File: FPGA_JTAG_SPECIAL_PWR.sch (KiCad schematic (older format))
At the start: 36 parts, among them J2 Reset_Switch, U900 GW1N-9LQ100

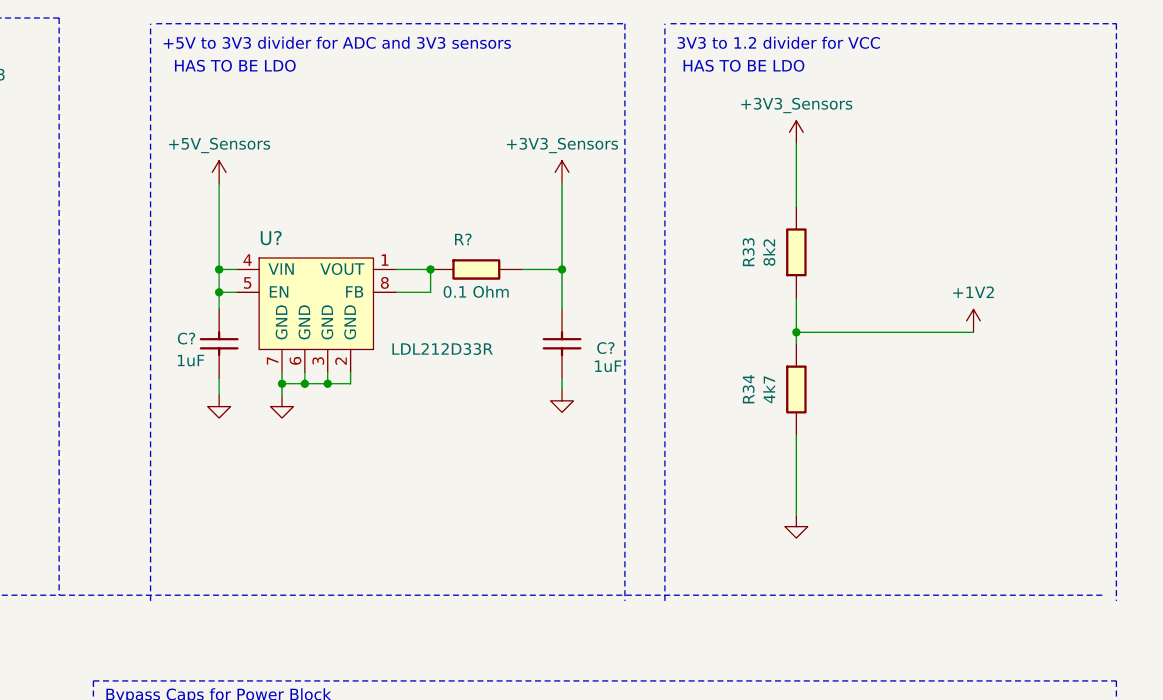
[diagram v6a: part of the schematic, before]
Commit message: TLV75512 ON fpga jtag special PWR sheet 7 Changed Q2 on Buzzer LEDs sheet 8 from N type to P type
TLV75512 ON fpga jtag special PWR sheet 7
Changed Q2 on Buzzer LEDs sheet 8 from N type to P type
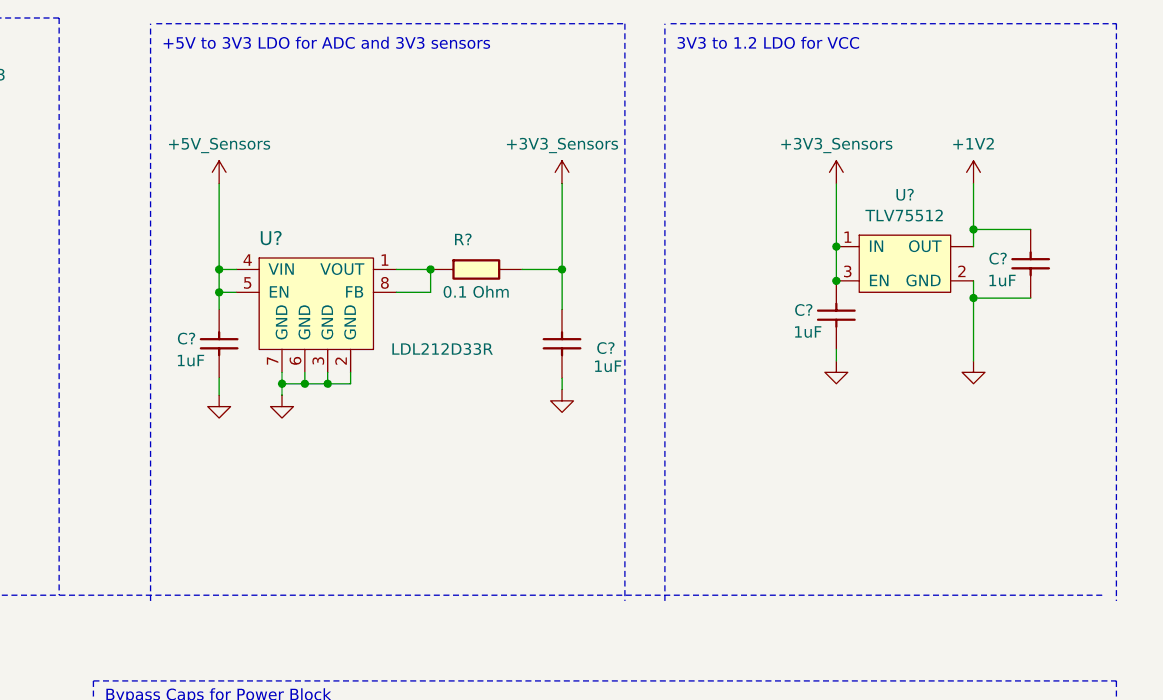
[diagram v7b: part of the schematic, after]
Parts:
- removed R33: 8k2_0603_Chip_Resistor,_1%,_0.1W, Resistor_SMD:R_0603_1608Metric, symbol OpenVent:8k2_0603_Chip_Resistor,_1%,_0.1W
- removed R34: 4k7_0603_Chip_Resistor,_1%,_0.1W, symbol OpenVent:4k7_0603_Chip_Resistor,_1%,_0.1W
- added C? (x2): 1uF_0603_Ceramic_Capacitor,_10%,_50V,_X5R, Capacitor_SMD:C_0603_1608Metric, symbol OpenVent:1uF_0603_Ceramic_Capacitor,_10%,_50V,_X5R
- added U?: TLV75512, symbol OpenVent:TLV75512
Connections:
- net +3.3V: now also C?.2, U?.1 (IN), U?.3 (EN)
- net +5V: now also C?.2, U?.~ (OUT)
- net GND: now also C?.1, C?.1, U?.2 (GND)
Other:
- note added: "+5V to 3V3 LDO for ADC and 3V3 sensors\n"
- note added: "3V3 to 1.2 LDO for VCC\n"
- note removed: "+5V to 3V3 divider for ADC and 3V3 sensors\n"
- note removed: "3V3 to 1.2 divider for VCC\n"
- note removed: "HAS TO BE LDO"
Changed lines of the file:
@@
 $EndComp
 Text Notes 9075 925  0    50   ~ 0
-3V3 to 1.2 divider for VCC\n
+3V3 to 1.2 LDO for VCC\n
 Text Notes 950  900  0    50   ~ 0
 FPGA Power Block
@@
 $EndComp
 Text Notes 6825 925  0    50   ~ 0
-+5V to 3V3 divider for ADC and 3V3 sensors\n
++5V to 3V3 LDO for ADC and 3V3 sensors\n
 Text GLabel 1700 5400 0    50   Input ~ 0
 TDI
@@
 	3625 1550 3625 1675
 $Comp
-L OpenVent:8k2_0603_Chip_Resistor,_1%,_0.1W R33
-U 1 1 5FCB78E3
-P 9500 1900
-F 0 "R33" H 9600 2007 50  0000 C CNN
-F 1 "8k2_0603_Chip_Resistor,_1%,_0.1W" H 9600 1900 50  0001 C CNN
-F 2 "Resistor_SMD:R_0603_1608Metric" H 9600 1900 50  0001 C CNN
-F 3 "" H 9500 1900 50  0001 C CNN
-F 4 "8k2" H 9600 1916 50  0000 C CNN "Val"
-F 5 "1%" H 9600 1900 50  0001 C CNN "Tolerance"
-F 6 "0.1W" H 9600 1900 50  0001 C CNN "Watt"
-	1    9500 1900
-	0    -1   -1   0
-$EndComp
-$Comp
-L OpenVent:4k7_0603_Chip_Resistor,_1%,_0.1W R34
-U 1 1 5FCBC9B7
-P 9700 2300
-F 0 "R34" H 9600 2607 50  0000 C CNN
-F 1 "4k7_0603_Chip_Resistor,_1%,_0.1W" H 9700 2300 50  0001 C CNN
-F 2 "" H 9700 2300 50  0001 C CNN
-F 3 "" H 9700 2300 60  0001 C CNN
-F 4 "4k7" H 9600 2516 50  0000 C CNN "Val"
-F 5 "1%" H 9700 2300 50  0001 C CNN "Tolerance"
-F 6 "0.1W" H 9700 2300 50  0001 C CNN "Watt"
-	1    9700 2300
-	0    -1   -1   0
-$EndComp
-$Comp
 L OpenVent:GND #PWR?
 U 1 1 5FCCFD82
@@
 L OpenVent:GND #PWR?
 U 1 1 5FCE591D
-P 9600 2950
+P 10375 2275
 AR Path="/5F8F8987/5FCE591D" Ref="#PWR?"  Part="1"
 AR Path="/5FB692C4/5FCE591D" Ref="#PWR067"  Part="1"
 AR Path="/5FBE8499/5FCE591D" Ref="#PWR071"  Part="1"
-F 0 "#PWR071" H 9600 2700 50  0001 C CNN
-F 1 "GND" H 9600 2800 50  0001 C CNN
-F 2 "" H 9600 2950 50  0001 C CNN
-F 3 "" H 9600 2950 50  0001 C CNN
-	1    9600 2950
-	1    0    0    -1
-$EndComp
-Wire Wire Line
-	9600 2600 9600 2950
-Wire Wire Line
-	9600 2200 9600 2150
+F 0 "#PWR071" H 10375 2025 50  0001 C CNN
+F 1 "GND" H 10375 2125 50  0001 C CNN
+F 2 "" H 10375 2275 50  0001 C CNN
+F 3 "" H 10375 2275 50  0001 C CNN
+	1    10375 2275
+	1    0    0    -1
+$EndComp
 $Comp
 L OpenVent:+1V2 #PWR072
 U 1 1 5FCE9B6E
-P 10375 2150
-F 0 "#PWR072" H 10375 2000 50  0001 C CNN
-F 1 "+1V2" H 10375 2323 50  0000 C CNN
-F 2 "" H 10375 2150 50  0001 C CNN
-F 3 "" H 10375 2150 50  0001 C CNN
-	1    10375 2150
-	1    0    0    -1
-$EndComp
-Wire Wire Line
-	9600 2150 10375 2150
-Connection ~ 9600 2150
-Wire Wire Line
-	9600 2150 9600 2000
+P 10375 1500
+F 0 "#PWR072" H 10375 1350 50  0001 C CNN
+F 1 "+1V2" H 10375 1673 50  0000 C CNN
+F 2 "" H 10375 1500 50  0001 C CNN
+F 3 "" H 10375 1500 50  0001 C CNN
+	1    10375 1500
+	1    0    0    -1
+$EndComp
 Wire Notes Line
 	6800 800  8850 800
@@
 	1    0    0    -1
 $EndComp
-Wire Wire Line
-	9600 1325 9600 1600
 $Comp
 L OpenVent:+3V3_Sensors #PWR?
 U 1 1 5FBD19B7
-P 9600 1325
+P 9775 1500
 AR Path="/5FBD19B7" Ref="#PWR?"  Part="1"
 AR Path="/5FB692C4/5FBD19B7" Ref="#PWR066"  Part="1"
 AR Path="/5FBE8499/5FBD19B7" Ref="#PWR070"  Part="1"
-F 0 "#PWR070" H 9600 1175 50  0001 C CNN
-F 1 "+3V3_Sensors" H 9600 1498 50  0000 C CNN
-F 2 "" H 9600 1325 50  0001 C CNN
-F 3 "" H 9600 1325 50  0001 C CNN
-	1    9600 1325
+F 0 "#PWR070" H 9775 1350 50  0001 C CNN
+F 1 "+3V3_Sensors" H 9775 1673 50  0000 C CNN
+F 2 "" H 9775 1500 50  0001 C CNN
+F 3 "" H 9775 1500 50  0001 C CNN
+	1    9775 1500
 	1    0    0    -1
 $EndComp
@@
 Wire Notes Line
 	6525 3675 6525 6450
-Text Notes 9100 1025 0    50   ~ 0
-HAS TO BE LDO
-Text Notes 6875 1025 0    50   ~ 0
-HAS TO BE LDO
 $Comp
 L OpenVent:12k_0603_Chip_Resistor,_1%,_0.1W R?
@@
 Wire Wire Line
 	8575 2400 8575 2350
+$Comp
+L OpenVent:TLV75512 U?
+U 1 1 5FF1B728
+P 9875 1775
+F 0 "U?" H 10075 2000 50  0000 C CNN
+F 1 "TLV75512" H 10075 1909 50  0000 C CNN
+F 2 "" H 10075 1975 50  0001 C CNN
+F 3 "" H 10075 1975 50  0001 C CNN
+	1    9875 1775
+	1    0    0    -1
+$EndComp
+Wire Wire Line
+	9775 1925 9775 1775
+$Comp
+L OpenVent:1uF_0603_Ceramic_Capacitor,_10%,_50V,_X5R C?
+U 1 1 5FF35DE7
+P 9675 2125
+AR Path="/5F99D63D/5FF35DE7" Ref="C?"  Part="1"
+AR Path="/5FBE8499/5FF35DE7" Ref="C?"  Part="1"
+F 0 "C?" V 9775 2125 50  0000 L BNN
+F 1 "1uF_0603_Ceramic_Capacitor,_10%,_50V,_X5R" V 9585 1935 50  0001 C CNN
+F 2 "Capacitor_SMD:C_0603_1608Metric" H 9585 1935 50  0001 C CNN
+F 3 "" H 9585 1935 50  0001 C CNN
+F 4 "10%" H 9675 2125 50  0001 C CNN "Tolerance"
+F 5 "1uF" V 9650 2150 50  0000 C CNN "Val"
+F 6 "50V" H 9675 2125 50  0001 C CNN "Voltage"
+	1    9675 2125
+	0    -1   -1   0
+$EndComp
+Connection ~ 9775 1925
+$Comp
+L OpenVent:GND #PWR?
+U 1 1 5FF36185
+P 9775 2275
+AR Path="/5F8F8987/5FF36185" Ref="#PWR?"  Part="1"
+AR Path="/5FB692C4/5FF36185" Ref="#PWR?"  Part="1"
+AR Path="/5FBE8499/5FF36185" Ref="#PWR?"  Part="1"
+F 0 "#PWR?" H 9775 2025 50  0001 C CNN
+F 1 "GND" H 9775 2125 50  0001 C CNN
+F 2 "" H 9775 2275 50  0001 C CNN
+F 3 "" H 9775 2275 50  0001 C CNN
+	1    9775 2275
+	1    0    0    -1
+$EndComp
+Wire Wire Line
+	9775 2275 9775 2225
+Connection ~ 9775 1775
+Wire Wire Line
+	9775 1500 9775 1775
+Wire Wire Line
+	10375 1775 10375 1700
+Wire Wire Line
+	10375 1925 10375 2000
+$Comp
+L OpenVent:1uF_0603_Ceramic_Capacitor,_10%,_50V,_X5R C?
+U 1 1 5FF46D9C
+P 10525 1900
+AR Path="/5F99D63D/5FF46D9C" Ref="C?"  Part="1"
+AR Path="/5FBE8499/5FF46D9C" Ref="C?"  Part="1"
+F 0 "C?" V 10625 1900 50  0000 L BNN
+F 1 "1uF_0603_Ceramic_Capacitor,_10%,_50V,_X5R" V 10435 1710 50  0001 C CNN
+F 2 "Capacitor_SMD:C_0603_1608Metric" H 10435 1710 50  0001 C CNN
+F 3 "" H 10435 1710 50  0001 C CNN
+F 4 "10%" H 10525 1900 50  0001 C CNN "Tolerance"
+F 5 "1uF" V 10500 1925 50  0000 C CNN "Val"
+F 6 "50V" H 10525 1900 50  0001 C CNN "Voltage"
+	1    10525 1900
+	0    -1   -1   0
+$EndComp
+Wire Wire Line
+	10625 1700 10375 1700
+Connection ~ 10375 1700
+Wire Wire Line
+	10375 1700 10375 1500
+Wire Wire Line
+	10625 2000 10375 2000
+Connection ~ 10375 2000
+Wire Wire Line
+	10375 2000 10375 2275
 $EndSCHEMATC
